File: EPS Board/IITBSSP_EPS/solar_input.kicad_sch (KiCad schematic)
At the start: 0 parts

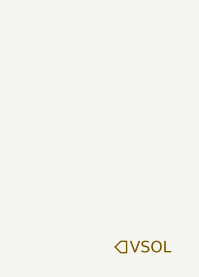
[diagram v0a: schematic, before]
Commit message: EPS Control Unit Dev and Final Schematic designed
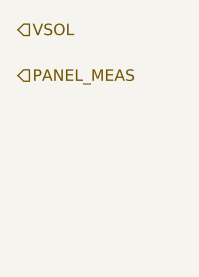
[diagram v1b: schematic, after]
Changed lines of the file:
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@@
 (kicad_sch (version 20230121) (generator eeschema)
   (paper "A4")
-  (hierarchical_label "VSOL" (shape input) (at 192.405 87.63 0) (fields_autoplaced)
+  (hierarchical_label "VSOL" (shape input) (at 181.61 63.5 0) (fields_autoplaced)
     (effects (font (size 1.27 1.27)) (justify left))
   )
+  (hierarchical_label "PANEL_MEAS" (shape input) (at 181.61 68.58 0) (fields_autoplaced)
+    (effects (font (size 1.27 1.27)) (justify left))
+  )
